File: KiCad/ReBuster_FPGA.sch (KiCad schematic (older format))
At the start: 26 parts, among them U1 10M02SCU169C8G, U2 LM1117-3.3

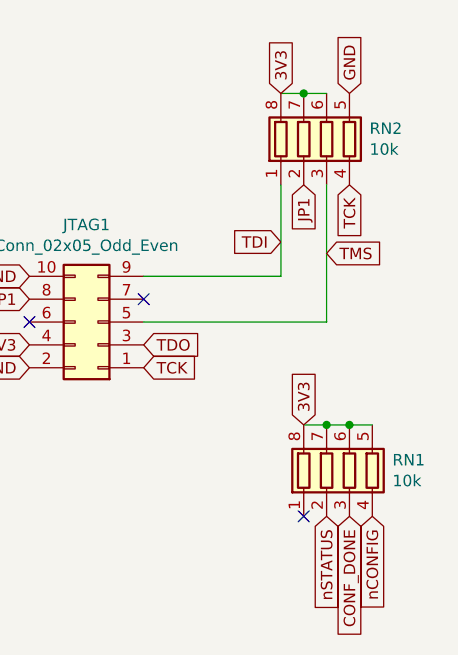
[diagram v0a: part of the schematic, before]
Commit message: Change RN1, RN2 value from 10k to 4.7k (CAY16A-4701F4LF) to follow Gowin JTAG recommended design.
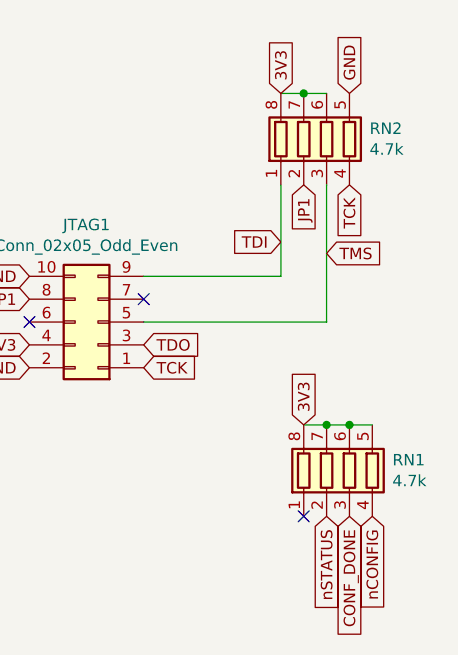
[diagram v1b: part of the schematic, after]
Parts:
- RN1, RN2: value 10k -> 4.7k
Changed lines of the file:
@@
 Text GLabel 3200 800  1    50   Input ~ 0
 3V3
-$Comp
-L ReBuster:10M02SCU169 U1
-U 1 1 60A0E571
-P 3400 3700
-F 0 "U1" H 3400 3750 60  0000 C CNN
-F 1 "10M02SCU169C8G" H 3400 3900 60  0000 C CNN
-F 2 "ReBuster:BGA-169_11.0x11.0mm_Layout13x13_P0.8mm_Ball0.5mm_Pad0.35mm_NSMD" H 3400 5900 60  0001 C CNN
-F 3 "" H 950 5800 60  0000 C CNN
-	1    3400 3700
-	1    0    0    -1
-$EndComp
 Wire Wire Line
 	2900 800  2900 1250
@@
 P 10550 1050
 F 0 "RN2" H 10738 1096 50  0000 L CNN
-F 1 "10k" H 10738 1005 50  0000 L CNN
+F 1 "4.7k" H 10738 1005 50  0000 L CNN
 F 2 "ReBuster:RESCAF80P320X160X60-8N" V 10825 1050 50  0001 C CNN
 F 3 "~" H 10550 1050 50  0001 C CNN
@@
 P 10650 2500
 F 0 "RN1" H 10838 2546 50  0000 L CNN
-F 1 "10k" H 10838 2455 50  0000 L CNN
+F 1 "4.7k" H 10838 2455 50  0000 L CNN
 F 2 "ReBuster:RESCAF80P320X160X60-8N" V 10925 2500 50  0001 C CNN
 F 3 "~" H 10650 2500 50  0001 C CNN
@@
 NoConn ~ 3450 6150
 NoConn ~ 5850 3450
+$Comp
+L ReBuster:10M02SCU169 U1
+U 1 1 60A0E571
+P 3400 3700
+F 0 "U1" H 3400 3750 60  0000 C CNN
+F 1 "10M02SCU169C8G" H 3400 3900 60  0000 C CNN
+F 2 "ReBuster:BGA-169_11.0x11.0mm_Layout13x13_P0.8mm_Ball0.5mm_Pad0.35mm_NSMD" H 3400 5900 60  0001 C CNN
+F 3 "" H 950 5800 60  0000 C CNN
+	1    3400 3700
+	1    0    0    -1
+$EndComp
 $EndSCHEMATC

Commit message: Change U1 from 10M02SCU169C8G to pin compatible Gowin FPGA GW1N-UV9UG169C6/I5
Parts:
- U1: value 10M02SCU169C8G -> GW1N-UV9UG169C6/I5; symbol ReBuster:10M02SCU169 -> ReBuster:GW1N-UV9UG169
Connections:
- wire segments 82 -> 80
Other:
- moved on the sheet: TP1

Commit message: Change back to a 10M02SCU169 FPGA
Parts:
- removed U1: GW1N-UV9UG169C6/I5, ReBuster:BGA-169_11.0x11.0mm_Layout13x13_P0.8mm_Ball0.5mm_Pad0.35mm_NSMD, symbol ReBuster:GW1N-UV9UG169
- added U1: 10M02SCU169, ReBuster:BGA-169_11.0x11.0mm_Layout13x13_P0.8mm_Ball0.5mm_Pad0.35mm_NSMD, symbol ReBuster:10M02SCU169
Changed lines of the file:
@@
 Text GLabel 3650 4600 3    50   Input ~ 0
 GND
-Text GLabel 3500 1300 1    50   Input ~ 0
+Text GLabel 3250 1300 1    50   Input ~ 0
 3V3
 Text GLabel 6050 4800 2    50   Input ~ 0
@@
 	7950 5300 8300 5300
 Wire Wire Line
-	3600 1300 3700 1300
-Connection ~ 3700 1300
-Wire Wire Line
-	3700 1300 3800 1300
-Connection ~ 3800 1300
-Wire Wire Line
-	3800 1300 3900 1300
-Connection ~ 3900 1300
-Wire Wire Line
-	3900 1300 4000 1300
-Connection ~ 4000 1300
-Wire Wire Line
-	4000 1300 4100 1300
-Connection ~ 4100 1300
-Wire Wire Line
-	4100 1300 4200 1300
-Connection ~ 4200 1300
-Wire Wire Line
-	4200 1300 4300 1300
-Connection ~ 4300 1300
-Wire Wire Line
-	4300 1300 4400 1300
-Wire Wire Line
-	3000 4600 3100 4600
-Connection ~ 3100 4600
-Wire Wire Line
-	3100 4600 3200 4600
-Connection ~ 3200 4600
-Wire Wire Line
-	3200 4600 3300 4600
-Connection ~ 3300 4600
-Wire Wire Line
-	3300 4600 3400 4600
-Connection ~ 3400 4600
-Wire Wire Line
-	3400 4600 3500 4600
-Connection ~ 3500 4600
-Wire Wire Line
-	3500 4600 3600 4600
-Connection ~ 3600 4600
-Wire Wire Line
-	3600 4600 3700 4600
-Connection ~ 3700 4600
-Wire Wire Line
-	3700 4600 3800 4600
-Connection ~ 3800 4600
-Wire Wire Line
-	3800 4600 3900 4600
-Connection ~ 3900 4600
-Wire Wire Line
-	3900 4600 4000 4600
-Connection ~ 4000 4600
-Wire Wire Line
-	4000 4600 4100 4600
-Connection ~ 4100 4600
-Wire Wire Line
-	4100 4600 4200 4600
-Connection ~ 4200 4600
-Wire Wire Line
-	4200 4600 4300 4600
-Connection ~ 4300 4600
-Wire Wire Line
-	4300 4600 4400 4600
-Connection ~ 4400 4600
-Wire Wire Line
-	4400 4600 4500 4600
-Wire Wire Line
 	3450 6200 3450 7000
 Text GLabel 1150 3900 0    50   Input ~ 0
@@
 NoConn ~ 6050 3500
 $Comp
-L ReBuster:GW1N-UV9UG169 U1
-U 1 1 60A0E571
+L ReBuster:10M02SCU169 U1
+U 1 1 699B1469
 P 3600 3750
-F 0 "U1" H 3600 3800 60  0000 C CNN
-F 1 "GW1N-UV9UG169C6/I5 " H 3600 3950 60  0000 C CNN
-F 2 "ReBuster:BGA-169_11.0x11.0mm_Layout13x13_P0.8mm_Ball0.5mm_Pad0.35mm_NSMD" H 3600 5950 60  0001 C CNN
-F 3 "" H 1150 5850 60  0000 C CNN
+F 0 "U1" H 3600 3900 60  0000 C CNN
+F 1 "10M02SCU169" H 3600 3750 60  0000 C CNN
+F 2 "ReBuster:BGA-169_11.0x11.0mm_Layout13x13_P0.8mm_Ball0.5mm_Pad0.35mm_NSMD" H 3600 4100 60  0001 C CNN
+F 3 "" H 5050 4950 60  0000 C CNN
 	1    3600 3750
 	1    0    0    -1
 $EndComp
 Wire Wire Line
-	2050 1300 2150 1300
-Connection ~ 2150 1300
-Wire Wire Line
-	2150 1300 2250 1300
-Connection ~ 2250 1300
-Wire Wire Line
-	2250 1300 2350 1300
-Connection ~ 2350 1300
-Wire Wire Line
-	2350 1300 2450 1300
-Connection ~ 2450 1300
-Wire Wire Line
-	2450 1300 2550 1300
-Connection ~ 2550 1300
-Wire Wire Line
-	2550 1300 2650 1300
-Connection ~ 2650 1300
-Wire Wire Line
-	2650 1300 2750 1300
-Connection ~ 2750 1300
-Wire Wire Line
-	2750 1300 2850 1300
-Connection ~ 2850 1300
-Wire Wire Line
-	2850 1300 2950 1300
-Connection ~ 2950 1300
-Wire Wire Line
-	2950 1300 3050 1300
-Connection ~ 3050 1300
-Wire Wire Line
-	3050 1300 3150 1300
-Connection ~ 3150 1300
-Wire Wire Line
-	3150 1300 3250 1300
-Connection ~ 3250 1300
-Wire Wire Line
-	3250 1300 3350 1300
-Wire Wire Line
-	3600 1300 3350 1300
+	3000 4600 3100 4600
+Wire Wire Line
+	1800 1300 1900 1300
+Connection ~ 3100 4600
+Wire Wire Line
+	3100 4600 3200 4600
+Connection ~ 3200 4600
+Wire Wire Line
+	3200 4600 3300 4600
+Connection ~ 3300 4600
+Wire Wire Line
+	3300 4600 3400 4600
+Connection ~ 3400 4600
+Wire Wire Line
+	3400 4600 3500 4600
+Connection ~ 3500 4600
+Wire Wire Line
+	3500 4600 3600 4600
+Connection ~ 3600 4600
+Wire Wire Line
+	3600 4600 3700 4600
+Connection ~ 3700 4600
+Wire Wire Line
+	3700 4600 3800 4600
+Connection ~ 3800 4600
+Wire Wire Line
+	3800 4600 3900 4600
+Connection ~ 3900 4600
+Wire Wire Line
+	3900 4600 4000 4600
+Connection ~ 4000 4600
+Wire Wire Line
+	4000 4600 4100 4600
+Connection ~ 4100 4600
+Wire Wire Line
+	4100 4600 4200 4600
+Connection ~ 4200 4600
+Wire Wire Line
+	4200 4600 4300 4600
+Connection ~ 4300 4600
+Wire Wire Line
+	4300 4600 4400 4600
+Connection ~ 4400 4600
+Wire Wire Line
+	4400 4600 4500 4600
+Connection ~ 1900 1300
+Wire Wire Line
+	1900 1300 2000 1300
+Connection ~ 2000 1300
+Wire Wire Line
+	2000 1300 2100 1300
+Connection ~ 2100 1300
+Wire Wire Line
+	2100 1300 2200 1300
+Connection ~ 2200 1300
+Wire Wire Line
+	2200 1300 2300 1300
+Connection ~ 2300 1300
+Wire Wire Line
+	2300 1300 2400 1300
+Connection ~ 2400 1300
+Wire Wire Line
+	2400 1300 2500 1300
+Connection ~ 2500 1300
+Wire Wire Line
+	2500 1300 2600 1300
+Connection ~ 2600 1300
+Wire Wire Line
+	2600 1300 2700 1300
+Connection ~ 2700 1300
+Wire Wire Line
+	2700 1300 2800 1300
+Connection ~ 2800 1300
+Wire Wire Line
+	2800 1300 2900 1300
+Connection ~ 2900 1300
+Wire Wire Line
+	2900 1300 3000 1300
+Connection ~ 3000 1300
+Wire Wire Line
+	3000 1300 3100 1300
+Connection ~ 3100 1300
+Wire Wire Line
+	3100 1300 3600 1300
 Connection ~ 3600 1300
-Connection ~ 3350 1300
+Wire Wire Line
+	3600 1300 3700 1300
+Connection ~ 3700 1300
+Wire Wire Line
+	3700 1300 3800 1300
+Connection ~ 3800 1300
+Wire Wire Line
+	3800 1300 3900 1300
+Connection ~ 3900 1300
+Wire Wire Line
+	3900 1300 4000 1300
+Connection ~ 4000 1300
+Wire Wire Line
+	4000 1300 4100 1300
+Connection ~ 4100 1300
+Wire Wire Line
+	4100 1300 4200 1300
+Connection ~ 4200 1300
+Wire Wire Line
+	4200 1300 4300 1300
+Connection ~ 4300 1300
+Wire Wire Line
+	4300 1300 4400 1300
 $EndSCHEMATC

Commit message: Add 74LVC2T45DC for handling DTACKn and MTACKn
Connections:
- net WAIT_FPGA: now also U1.H8 (IO_5); no longer U1.K1 (IO_2)
- no-connect marks 24 -> 23
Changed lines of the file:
@@
 Text GLabel 2950 6200 3    50   Output ~ 0
 DBR16_FPGA
-Text GLabel 1150 4800 0    50   Input ~ 0
+Text GLabel 5350 6200 3    50   Input ~ 0
 WAIT_FPGA
 Text GLabel 1150 3600 0    50   BiDi ~ 0
@@
 NoConn ~ 4950 6200
 NoConn ~ 5150 6200
-NoConn ~ 5350 6200
 NoConn ~ 5450 6200
 NoConn ~ 6050 5800
@@
 Wire Wire Line
 	8100 1500 8500 1500
-Text GLabel 3450 6900 0    50   Input ~ 0
-TP1
 Wire Wire Line
 	10550 2300 10650 2300
@@
 Text GLabel 6050 5400 2    50   Input ~ 0
 EBR2_FPGA
-$Comp
-L Connector:TestPoint_Small TP1
-U 1 1 655D4DC6
-P 3450 7000
-F 0 "TP1" H 3498 7000 50  0000 L CNN
-F 1 "TestPoint_Small" H 3498 6955 50  0001 L CNN
-F 2 "TestPoint:TestPoint_Pad_1.5x1.5mm" H 3650 7000 50  0001 C CNN
-F 3 "~" H 3650 7000 50  0001 C CNN
-	1    3450 7000
-	1    0    0    -1
-$EndComp
 Text GLabel 6050 3000 2    50   Input ~ 0
 GND
@@
 Wire Wire Line
 	7950 5300 8300 5300
-Wire Wire Line
-	3450 6200 3450 7000
 Text GLabel 1150 3900 0    50   Input ~ 0
 3V3
@@
 Wire Wire Line
 	4300 1300 4400 1300
+Text GLabel 3400 7300 0    50   Input ~ 0
+DIR_U4
+Wire Wire Line
+	3450 6200 3450 7000
+$Comp
+L Connector:TestPoint_Small TP1
+U 1 1 655D4DC6
+P 3450 7000
+F 0 "TP1" H 3498 7000 50  0000 L CNN
+F 1 "TestPoint_Small" H 3498 6955 50  0001 L CNN
+F 2 "TestPoint:TestPoint_Pad_1.5x1.5mm" H 3650 7000 50  0001 C CNN
+F 3 "~" H 3650 7000 50  0001 C CNN
+	1    3450 7000
+	1    0    0    -1
+$EndComp
+Text GLabel 3450 6900 0    50   Input ~ 0
+TP1
 $EndSCHEMATC

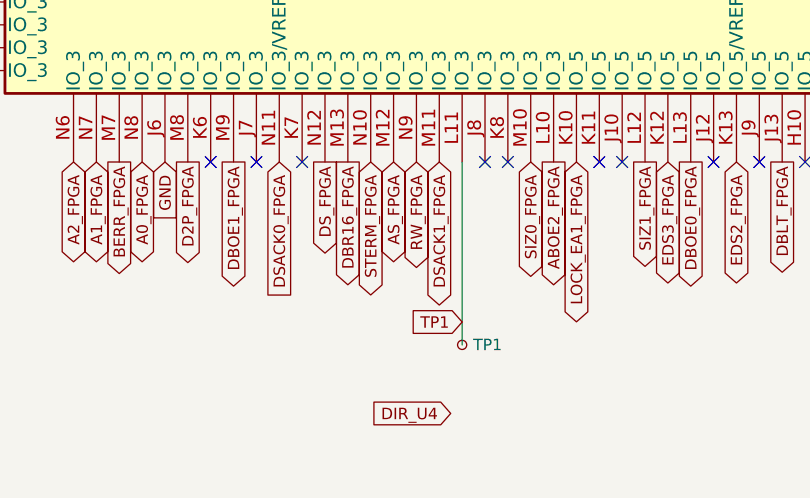
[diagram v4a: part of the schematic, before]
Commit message: Route AS,SIZ1,SIZ0,RW to U4 (SN74LVC16T245DGVR) and FPGA
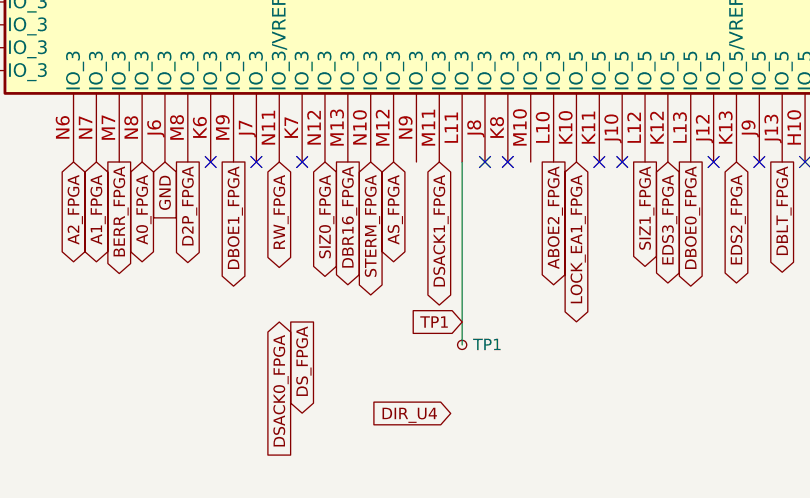
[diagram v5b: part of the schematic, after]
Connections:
- net DSACK0_FPGA: no longer U1.N11 (IO_3/VREFB3N0)
- net DS_FPGA: no longer U1.N12 (IO_3)
- net RW_FPGA: now also U1.N11 (IO_3/VREFB3N0); no longer U1.N9 (IO_3)
- net SIZ0_FPGA: now also U1.N12 (IO_3); no longer U1.M10 (IO_3)
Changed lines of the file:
@@
 Text GLabel 1150 4200 0    50   Output ~ 0
 SBG_FPGA
-Text GLabel 3250 6200 3    50   BiDi ~ 0
+Text GLabel 2650 6200 3    50   BiDi ~ 0
 RW_FPGA
-Text GLabel 3750 6200 3    50   BiDi ~ 0
+Text GLabel 2850 6200 3    50   BiDi ~ 0
 SIZ0_FPGA
 Text GLabel 3050 6200 3    50   BiDi ~ 0
@@
 Text GLabel 3350 6200 3    50   BiDi ~ 0
 DSACK1_FPGA
-Text GLabel 2650 6200 3    50   Input ~ 0
+Text GLabel 2650 6900 3    50   Input ~ 0
 DSACK0_FPGA
-Text GLabel 2850 6200 3    50   Output ~ 0
+Text GLabel 2750 6900 3    50   Output ~ 0
 DS_FPGA
 Text GLabel 3150 6200 3    50   BiDi ~ 0

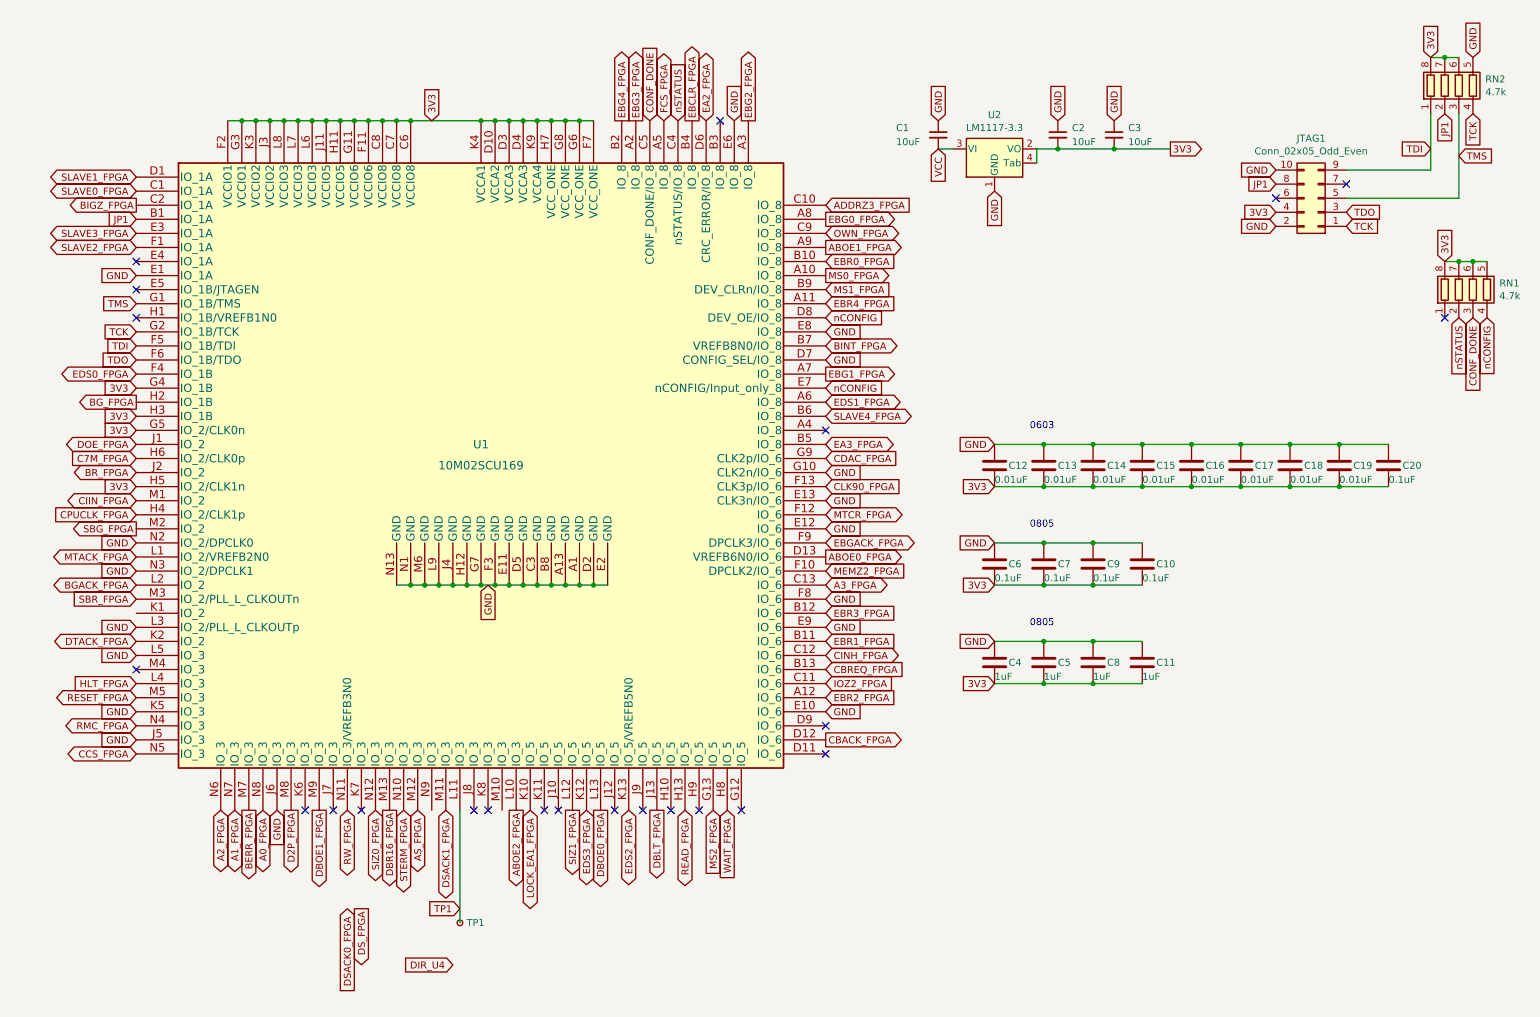
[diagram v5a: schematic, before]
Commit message: Route EDS1, CCS, FCS signals to U4 (SN74LVC16T245DGVR) and FPGA
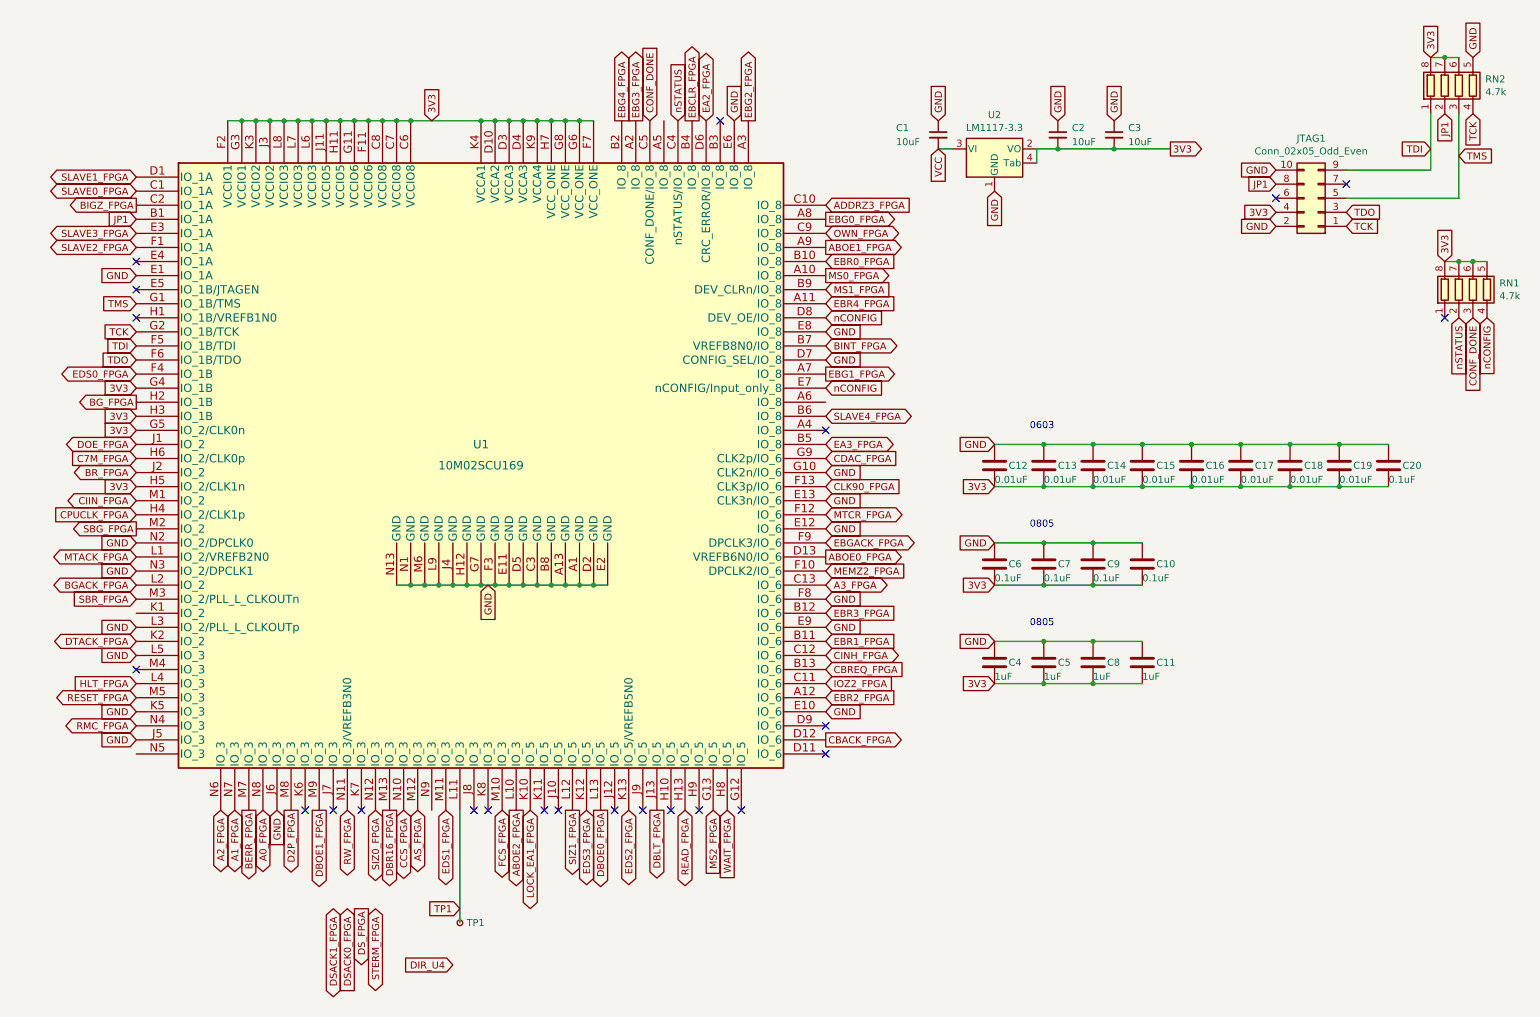
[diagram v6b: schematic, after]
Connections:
- net CCS_FPGA: now also U1.N10 (IO_3); no longer U1.N5 (IO_3)
- net DSACK1_FPGA: no longer U1.M11 (IO_3)
- net EDS1_FPGA: now also U1.M11 (IO_3); no longer U1.A6 (IO_8)
- net FCS_FPGA: now also U1.M10 (IO_3); no longer U1.A5 (IO_8)
- net STERM_FPGA: no longer U1.N10 (IO_3)
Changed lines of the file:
@@
 Text GLabel 6050 3100 2    50   Output ~ 0
 EBG1_FPGA
-Text GLabel 6050 3300 2    50   BiDi ~ 0
+Text GLabel 3350 6200 3    50   BiDi ~ 0
 EDS1_FPGA
-Text GLabel 4900 1300 1    50   BiDi ~ 0
+Text GLabel 3750 6200 3    50   BiDi ~ 0
 FCS_FPGA
 Text GLabel 5500 1300 1    50   Output ~ 0
@@
 Text GLabel 1150 5600 0    50   BiDi ~ 0
 RMC_FPGA
-Text GLabel 1150 5800 0    50   BiDi ~ 0
+Text GLabel 3050 6200 3    50   BiDi ~ 0
 CCS_FPGA
 Text GLabel 1750 6200 3    50   BiDi ~ 0
@@
 Text GLabel 2850 6200 3    50   BiDi ~ 0
 SIZ0_FPGA
-Text GLabel 3050 6200 3    50   BiDi ~ 0
+Text GLabel 2850 6900 3    50   BiDi ~ 0
 STERM_FPGA
-Text GLabel 3350 6200 3    50   BiDi ~ 0
+Text GLabel 2550 6900 3    50   BiDi ~ 0
 DSACK1_FPGA
 Text GLabel 2650 6900 3    50   Input ~ 0
